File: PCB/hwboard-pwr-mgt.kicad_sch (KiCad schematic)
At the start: 0 parts

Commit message: add charger and fuel gauge ic
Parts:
- added U3: BQ25622ERYKR, hwboard-bike-computer:BQ25622ERYKR, symbol hwboard-bike-computer:BQ25622ERYKR
- added U4: MAX17048G+, Package_DFN_QFN:TDFN-8-1EP_2x2mm_P0.5mm_EP0.8x1.2mm, symbol hwboard-bike-computer:MAX17048G+

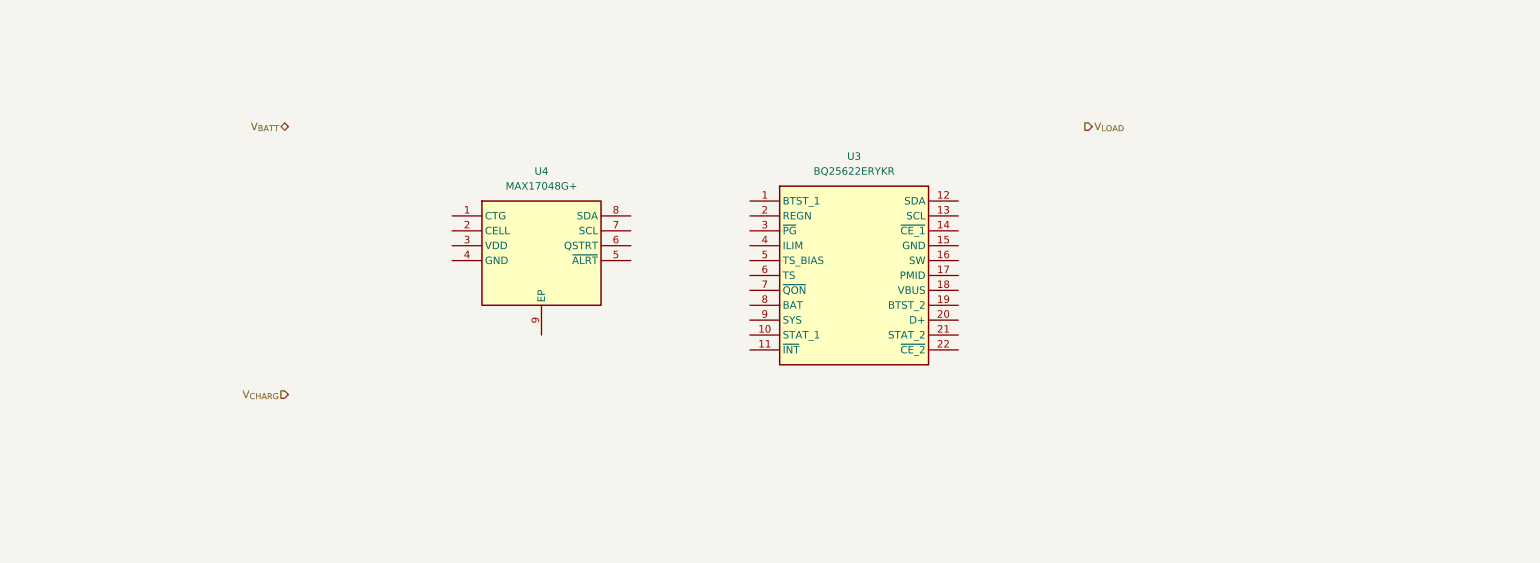
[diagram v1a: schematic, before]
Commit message: schematic for charger and fuel gauge
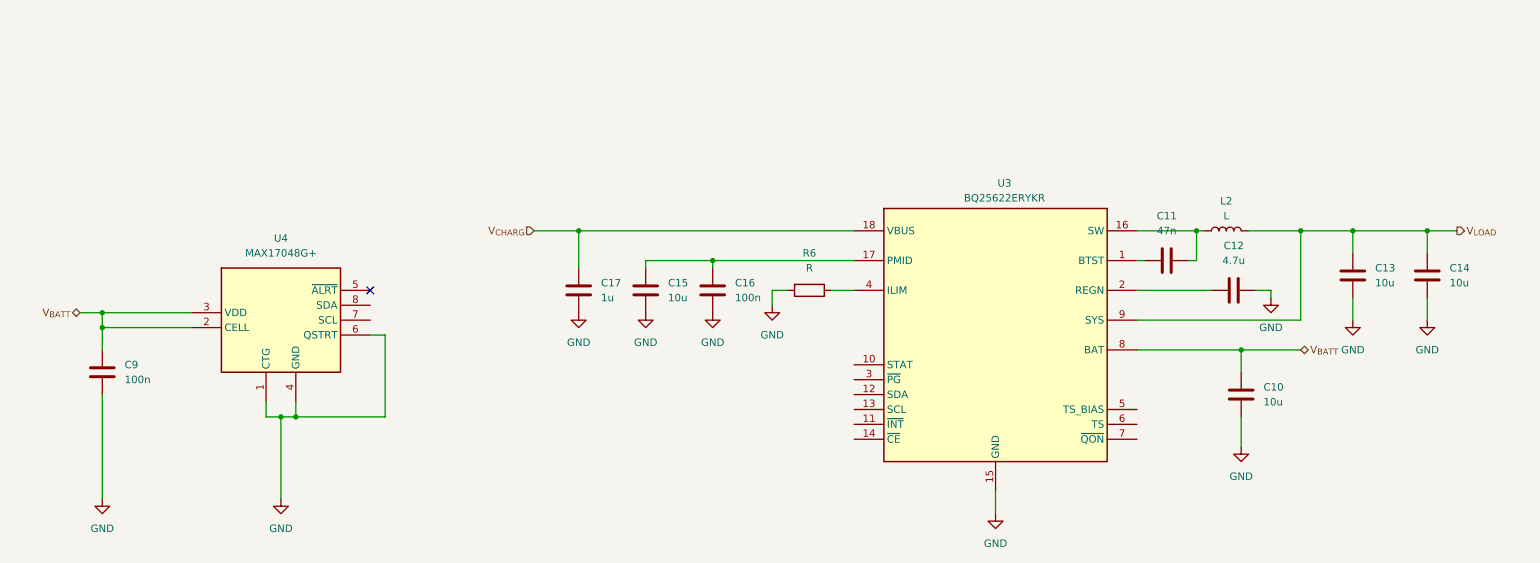
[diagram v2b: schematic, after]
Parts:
- added C10, C13, C14, C15: 10u, symbol Device:C
- added C11: 47n, symbol Device:C
- added C12: 4.7u, symbol Device:C
- added C16, C9: 100n, symbol Device:C
- added C17: 1u, symbol Device:C
- added L2: L, symbol Device:L
- added R6: R, symbol Device:R
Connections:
- net V_{BATT}: now also U3.8 (BAT), U4.2 (CELL), U4.3 (VDD), C10.1, C9.1
- net V_{CHARG}: now also U3.18 (VBUS), C17.1
- net V_{LOAD}: now also U3.9 (SYS), C13.1, C14.1, L2.2
- net at U3.1 (BTST): now also C11.1
- net GND: now reaches U3.15 (GND)
- net GND: now also U4.1 (CTG), U4.4 (GND), U4.6 (QSTRT), U4.9 (EP), C10.2, C12.1, C13.2, C14.2, C15.2, C16.2, C17.2, C9.2, R6.2
- net at U3.16 (SW): now also C11.2, L2.1
- net at U3.17 (PMID): now also C15.1, C16.1
- net at U3.2 (REGN): now also C12.2
- net at U3.4 (ILIM): now also R6.1
- no-connect marks 0 -> 1

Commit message: Update with gnss
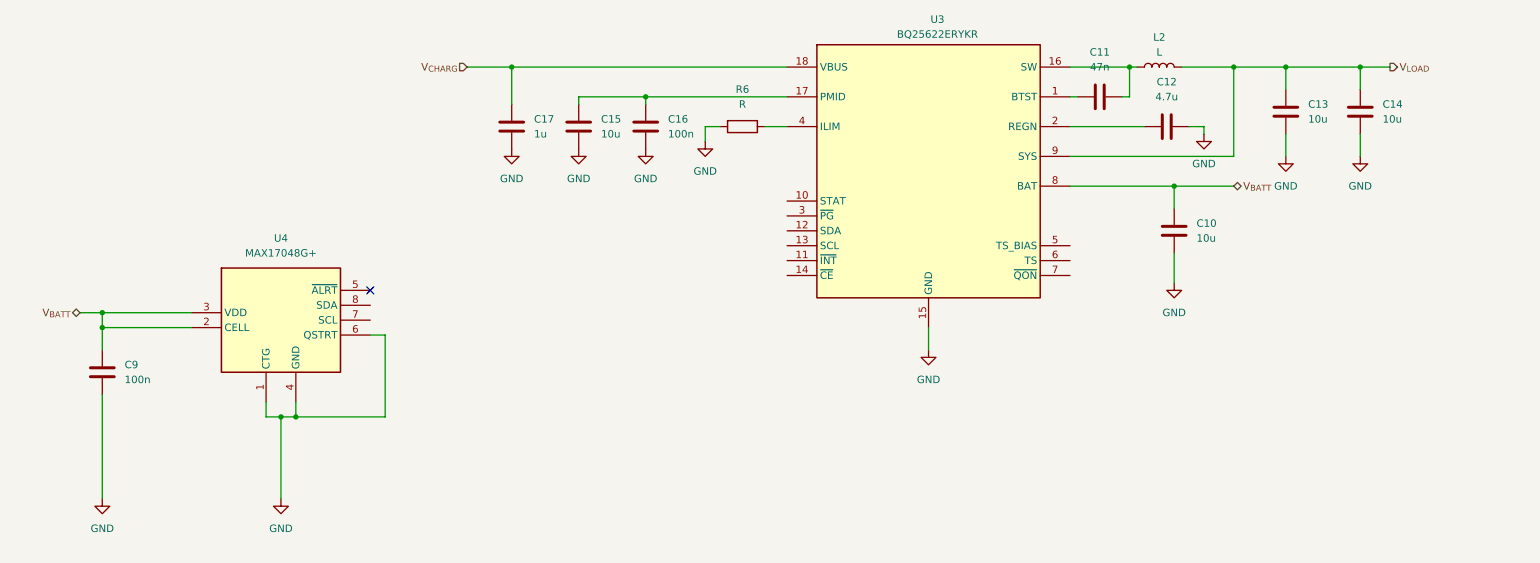
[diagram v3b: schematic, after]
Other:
- moved on the sheet: C10, C11, C12, C13, C14, C15, C16, C17, L2, R6, U3

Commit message: add resistive touch IC
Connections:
- net POWER_{I2C}.SDA: now reaches U3.12 (SDA)
- net POWER_{I2C}.SDA: now also U4.8 (SDA)
- net POWER_{I2C}.SCL: now reaches U3.13 (SCL)
- net POWER_{I2C}.SCL: now also U4.7 (SCL)
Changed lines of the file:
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@@
 		(at 91.44 96.52)
 	)
+	(bus_entry
+		(at 109.22 99.06)
+		(size -2.54 2.54)
+		(stroke
+			(width 0)
+			(type default)
+		)
+	)
+	(bus_entry
+		(at 109.22 96.52)
+		(size -2.54 2.54)
+		(stroke
+			(width 0)
+			(type default)
+		)
+	)
+	(bus_entry
+		(at 144.78 86.36)
+		(size 2.54 2.54)
+		(stroke
+			(width 0)
+			(type default)
+		)
+	)
+	(bus_entry
+		(at 144.78 83.82)
+		(size 2.54 2.54)
+		(stroke
+			(width 0)
+			(type default)
+		)
+	)
 	(wire
 		(pts
@@
 	(wire
 		(pts
+			(xy 147.32 88.9) (xy 162.56 88.9)
+		)
+		(stroke
+			(width 0)
+			(type default)
+		)
+	)
+	(wire
+		(pts
 			(xy 220.98 63.5) (xy 220.98 58.42)
 		)
@@
 	(wire
 		(pts
+			(xy 147.32 86.36) (xy 162.56 86.36)
+		)
+		(stroke
+			(width 0)
+			(type default)
+		)
+	)
+	(wire
+		(pts
 			(xy 107.95 58.42) (xy 115.57 58.42)
 		)
@@
 	(wire
 		(pts
+			(xy 91.44 101.6) (xy 106.68 101.6)
+		)
+		(stroke
+			(width 0)
+			(type default)
+		)
+	)
+	(wire
+		(pts
 			(xy 127 64.77) (xy 127 63.5)
 		)
@@
 		)
 	)
+	(bus
+		(pts
+			(xy 144.78 83.82) (xy 144.78 86.36)
+		)
+		(stroke
+			(width 0)
+			(type default)
+		)
+	)
 	(wire
 		(pts
@@
 	(wire
 		(pts
+			(xy 91.44 99.06) (xy 106.68 99.06)
+		)
+		(stroke
+			(width 0)
+			(type default)
+		)
+	)
+	(wire
+		(pts
 			(xy 115.57 58.42) (xy 115.57 64.77)
 		)
@@
 		)
 	)
+	(bus
+		(pts
+			(xy 142.24 83.82) (xy 144.78 83.82)
+		)
+		(stroke
+			(width 0)
+			(type default)
+		)
+	)
 	(wire
 		(pts
@@
 		)
 	)
+	(bus
+		(pts
+			(xy 110.49 96.52) (xy 109.22 96.52)
+		)
+		(stroke
+			(width 0)
+			(type default)
+		)
+	)
 	(wire
 		(pts
@@
 		)
 	)
+	(bus
+		(pts
+			(xy 109.22 96.52) (xy 109.22 99.06)
+		)
+		(stroke
+			(width 0)
+			(type default)
+		)
+	)
 	(wire
 		(pts
@@
 			(width 0)
 			(type default)
+		)
+	)
+	(label "POWER_{I2C}.SCL"
+		(at 93.98 101.6 0)
+		(effects
+			(font
+				(size 1.27 1.27)
+			)
+			(justify left bottom)
+		)
+	)
+	(label "POWER_{I2C}.SDA"
+		(at 93.98 99.06 0)
+		(effects
+			(font
+				(size 1.27 1.27)
+			)
+			(justify left bottom)
+		)
+	)
+	(label "POWER_{I2C}.SCL"
+		(at 161.29 88.9 180)
+		(effects
+			(font
+				(size 1.27 1.27)
+			)
+			(justify right bottom)
+		)
+	)
+	(label "POWER_{I2C}.SDA"
+		(at 161.29 86.36 180)
+		(effects
+			(font
+				(size 1.27 1.27)
+			)
+			(justify right bottom)
 		)
 	)
@@
 		)
 	)
+	(hierarchical_label "POWER_{I2C}{I2C}"
+		(shape bidirectional)
+		(at 142.24 83.82 180)
+		(effects
+			(font
+				(size 1.27 1.27)
+			)
+			(justify right)
+		)
+	)
 	(hierarchical_label "V_{BATT}"
 		(shape bidirectional)
@@
 		(effects
 			(font
+				(size 1.27 1.27)
+			)
+			(justify left)
+		)
+	)
+	(hierarchical_label "POWER_{I2C}{I2C}"
+		(shape bidirectional)
+		(at 110.49 96.52 0)
+		(effects
+			(font

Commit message: add maybe layout and pcb for screen
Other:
- moved on the sheet: L2
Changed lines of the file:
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@@
 	(wire
 		(pts
-			(xy 220.98 58.42) (xy 222.25 58.42)
+			(xy 220.98 58.42) (xy 226.06 58.42)
 		)
 		(stroke
@@
 	(wire
 		(pts
-			(xy 238.76 58.42) (xy 229.87 58.42)
+			(xy 238.76 58.42) (xy 233.68 58.42)
 		)
 		(stroke
@@
 		(on_board yes)
 		(dnp no)
-		(fields_autoplaced yes)
 		(property "Reference" "C11"
-			(at 215.9 55.88 90)
+			(at 215.9 54.61 90)
 			(effects
 				(font
@@
 		)
 		(property "Value" "47n"
-			(at 215.9 58.42 90)
+			(at 215.9 57.15 90)
 			(effects
 				(font
@@
 	(symbol
 		(lib_id "Device:L")
-		(at 226.06 58.42 90)
+		(at 229.87 58.42 90)
 		(unit 1)
 		(exclude_from_sim no)
@@
 		(fields_autoplaced yes)
 		(property "Reference" "L2"
-			(at 226.06 53.34 90)
+			(at 229.87 53.34 90)
 			(effects
 				(font
@@
 		)
 		(property "Value" "L"
-			(at 226.06 55.88 90)
+			(at 229.87 55.88 90)
 			(effects
 				(font
@@
 		)
 		(property "Footprint" ""
-			(at 226.06 58.42 0)
+			(at 229.87 58.42 0)
 			(effects
 				(font
@@
 		)
 		(property "Datasheet" "~"
-			(at 226.06 58.42 0)
+			(at 229.87 58.42 0)
 			(effects
 				(font
@@
 		)
 		(property "Description" "Inductor"
-			(at 226.06 58.42 0)
-			(effects
-				(font
+			(at 229.87 58.42 0)
+			(effects
+				(font
